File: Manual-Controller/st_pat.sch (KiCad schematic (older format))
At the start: 20 parts, among them J4 BATTERY, SW1 SW_PWR, SW2 BTN_RST, SW3 BTN, SW4 BTN, SW5 BTN, U1 GPS_Breakout_746, U2 FEATHER_M0_BASIC_PROTO, U4 Sharp_Display_4694

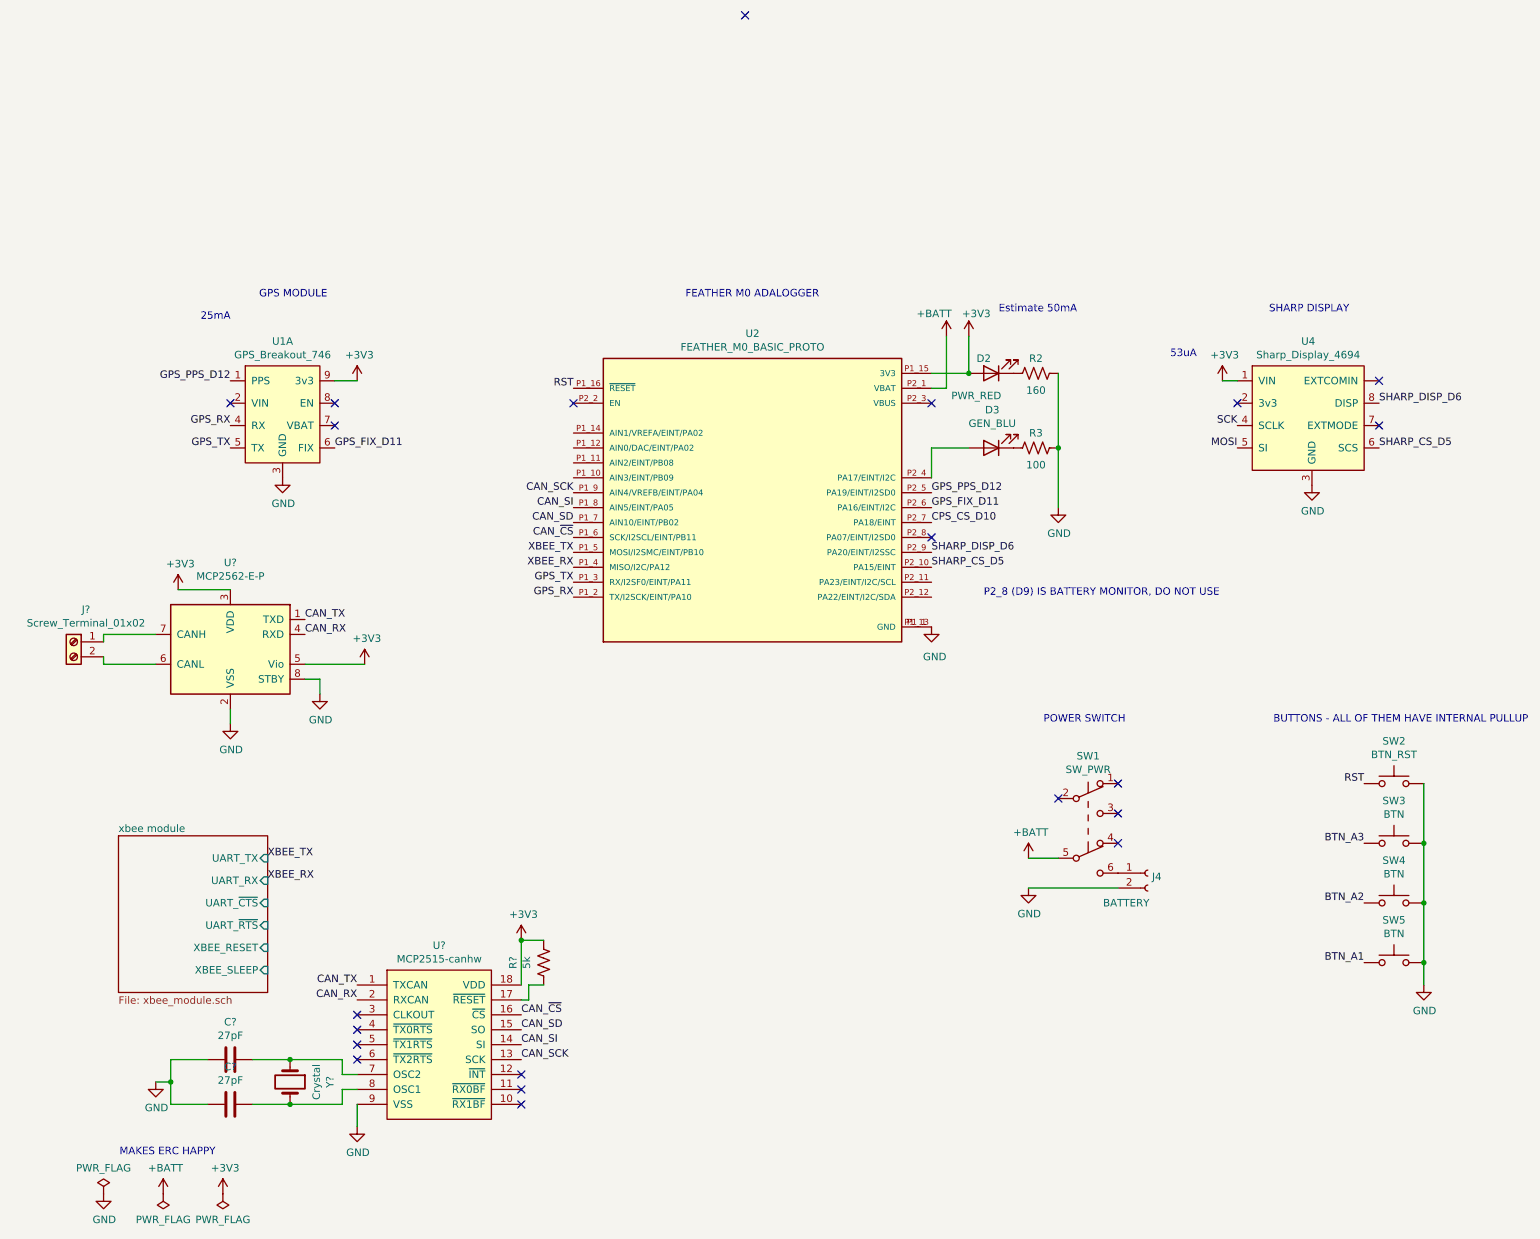
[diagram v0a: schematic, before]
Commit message: CAN support for featherboard
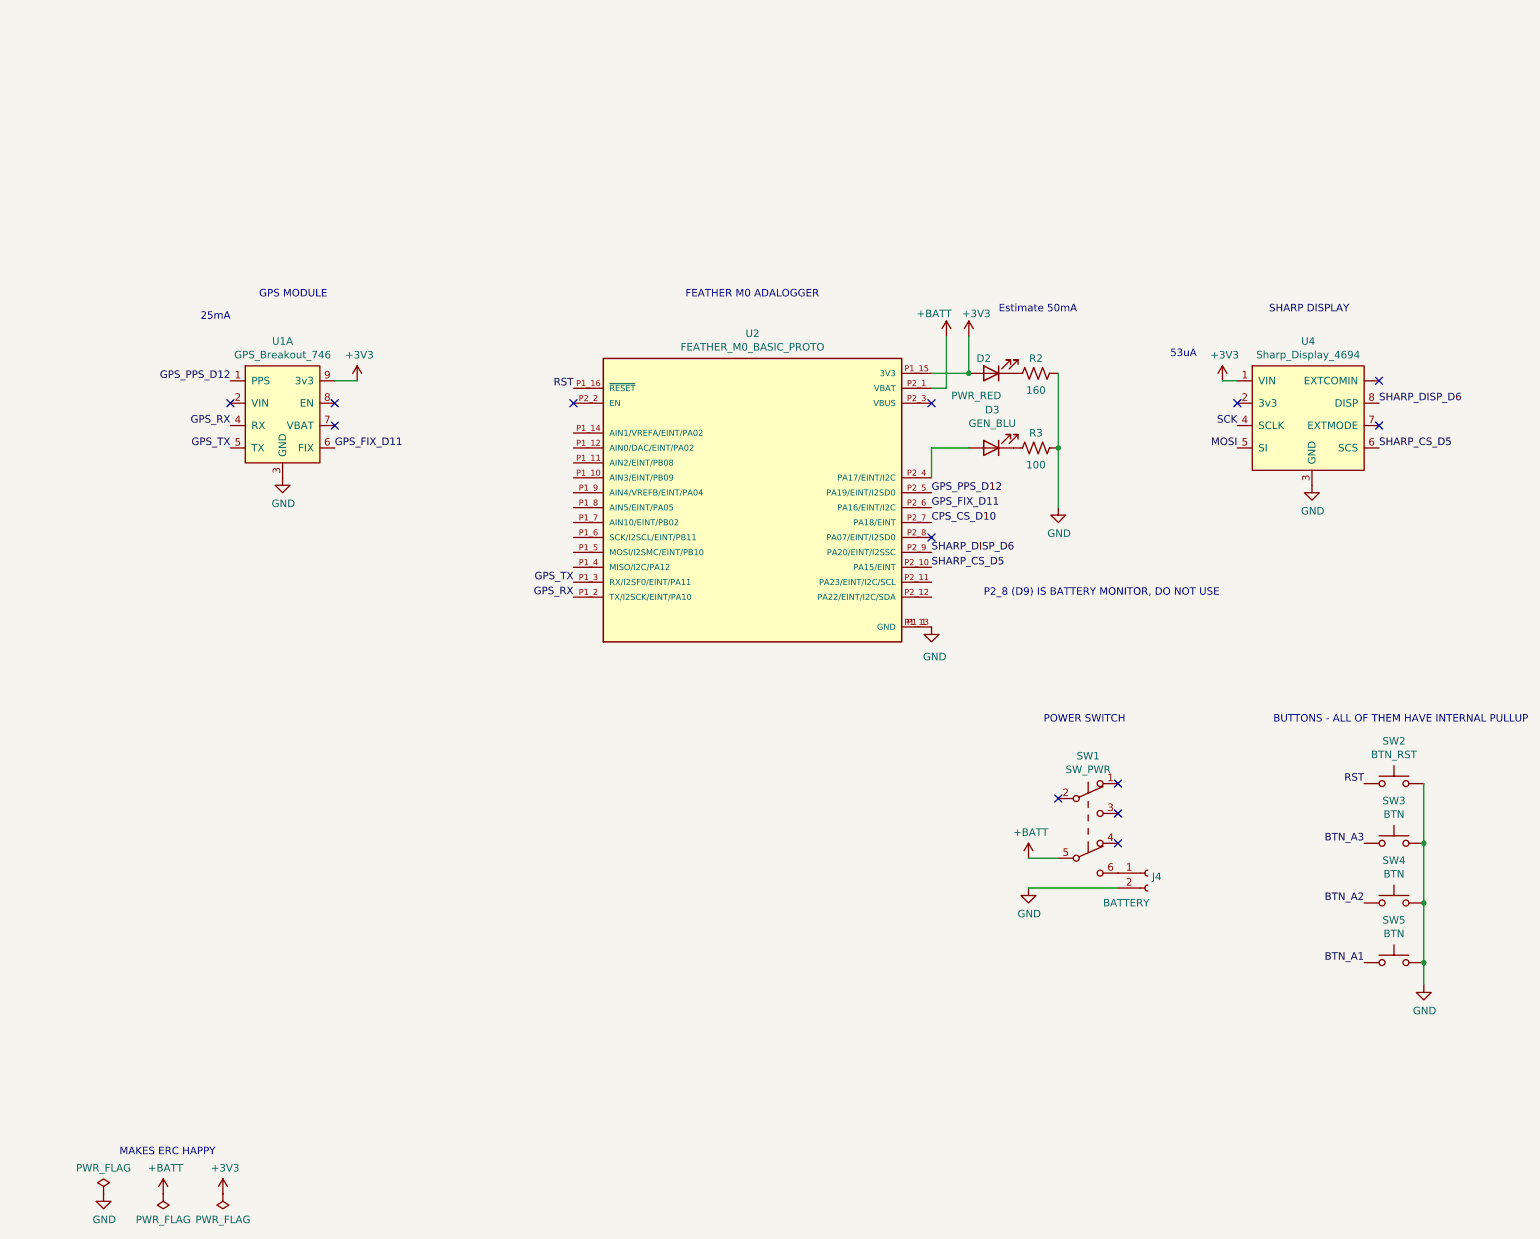
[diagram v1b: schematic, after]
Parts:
- removed C? (x2): 27pF, symbol Device:C
- removed J?: Screw_Terminal_01x02, symbol Connector:Screw_Terminal_01x02
- removed R?: 5k, symbol Device:R_US
- removed U?: MCP2515-canhw, symbol payload2022_custom:MCP2515-canhw
- removed U?: MCP2562-E-P, Package_DIP:DIP-8_W7.62mm, symbol Interface_CAN_LIN:MCP2562-E-P
- removed Y?: Crystal, symbol Device:Crystal
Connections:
- net CAN_SCK: no longer names the net of U2.P1_9 (AIN4/VREFB/EINT/PA04)
- net CAN_SD: no longer names the net of U2.P1_7 (AIN10/EINT/PB02)
- net CAN_SI: no longer names the net of U2.P1_8 (AIN5/EINT/PA05)
- net CAN_~CS: no longer names the net of U2.P1_6 (SCK/I2SCL/EINT/PB11)
- net XBEE_RX: no longer names the net of U2.P1_4 (MISO/I2C/PA12)
- net XBEE_TX: no longer names the net of U2.P1_5 (MOSI/I2SMC/EINT/PB10)
- no-connect marks 21 -> 13
